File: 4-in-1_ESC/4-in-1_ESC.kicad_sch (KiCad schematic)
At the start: 12 parts, among them J5 BLDC Solder Pads

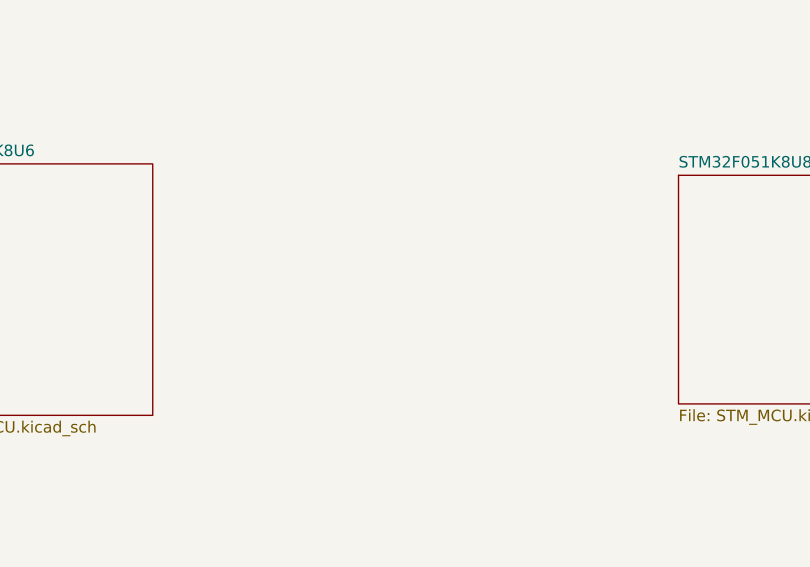
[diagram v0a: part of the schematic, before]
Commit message: Schematic Updates
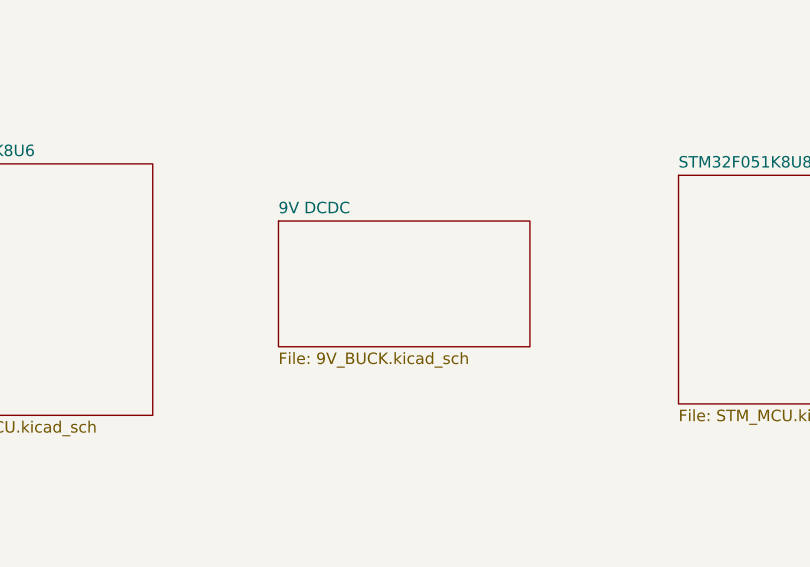
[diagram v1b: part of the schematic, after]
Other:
- added sheet 9V DCDC (9V_BUCK.kicad_sch)
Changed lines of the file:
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@@
+		)
+	)
+	(sheet
+		(at 132.08 78.74)
+		(size 27.94 13.97)
+		(exclude_from_sim no)
+		(in_bom yes)
+		(on_board yes)
+		(dnp no)
+		(fields_autoplaced yes)
+		(stroke
+			(width 0.1524)
+			(type solid)
+		)
+		(fill
+			(color 0 0 0 0)
+		)
+		(property "Sheetname" "9V DCDC"
+			(at 132.08 78.0284 0)
+			(show_name no)
+			(do_not_autoplace no)
+			(effects
+				(font
+					(size 1.27 1.27)
+				)
+				(justify left bottom)
+			)
+		)
+		(property "Sheetfile" "9V_BUCK.kicad_sch"
+			(at 132.08 93.2946 0)
+			(show_name no)
+			(do_not_autoplace no)
+			(effects
+				(font
+					(size 1.27 1.27)
+				)
+				(justify left top)
+			)
+		)
+		(instances
+			(project "4-in-1_ESC"
+				(path "/885456b2-b92d-459f-a061-5f970a420f96"
+					(page "11")
+				)
+			)
 		)
 	)

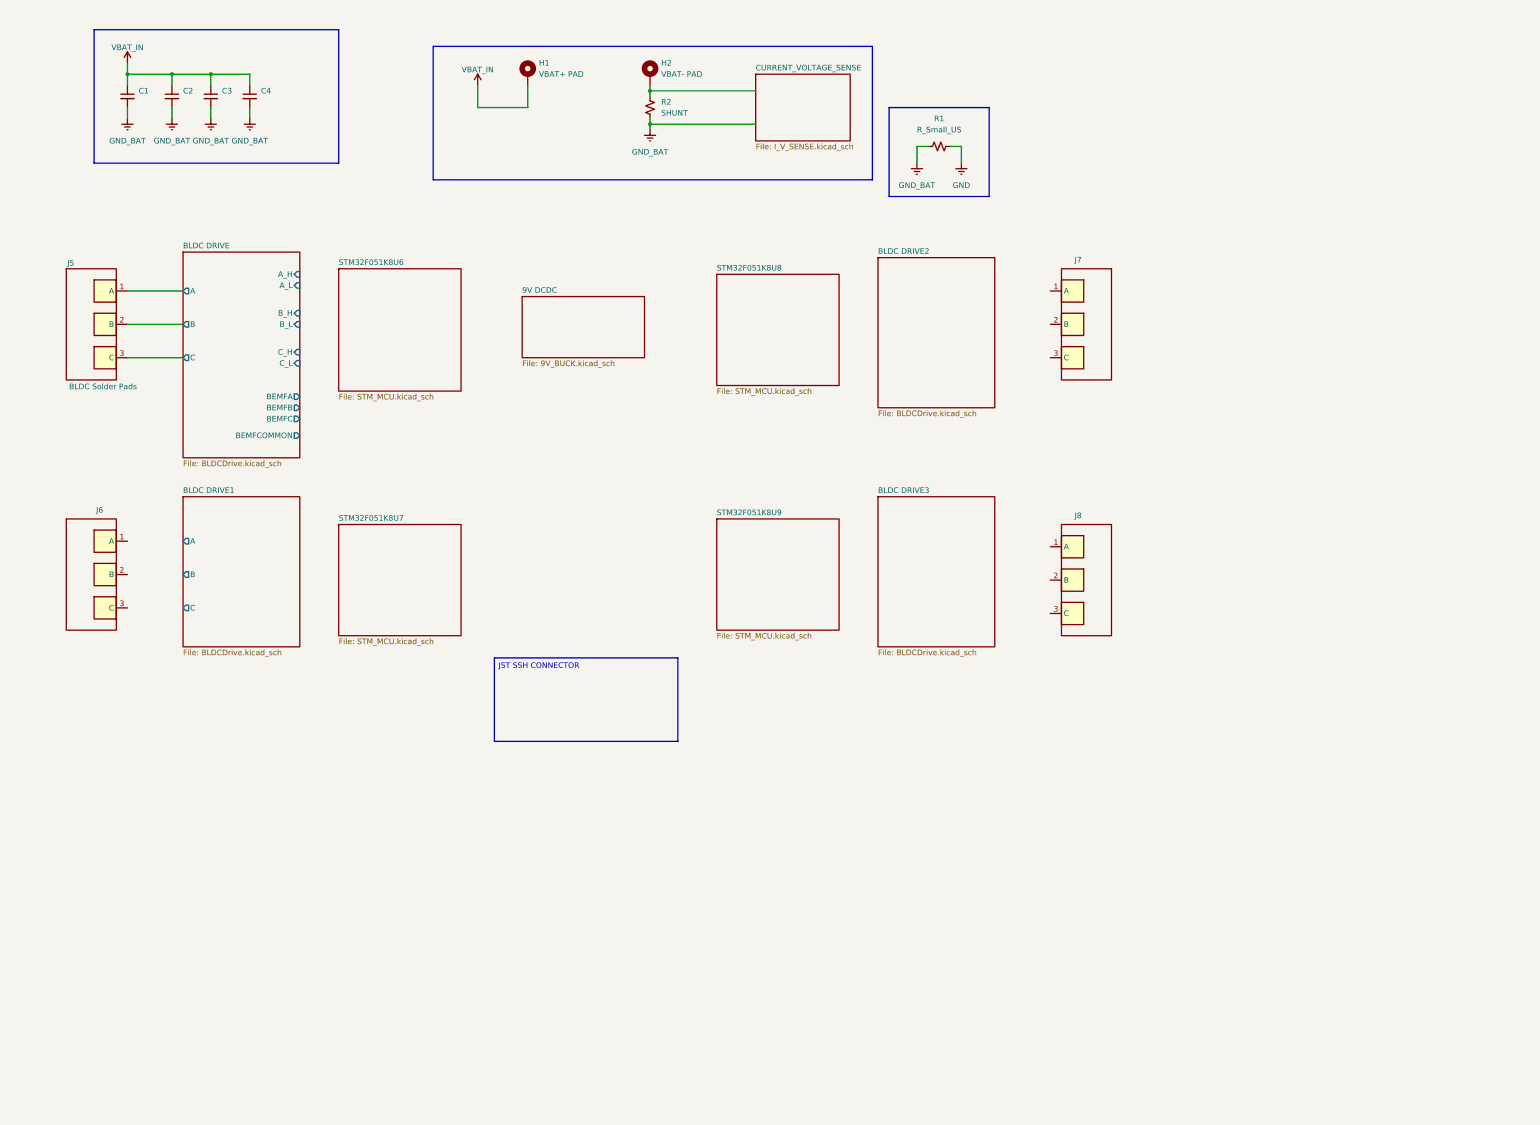
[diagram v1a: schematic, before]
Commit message: Schematic Updates
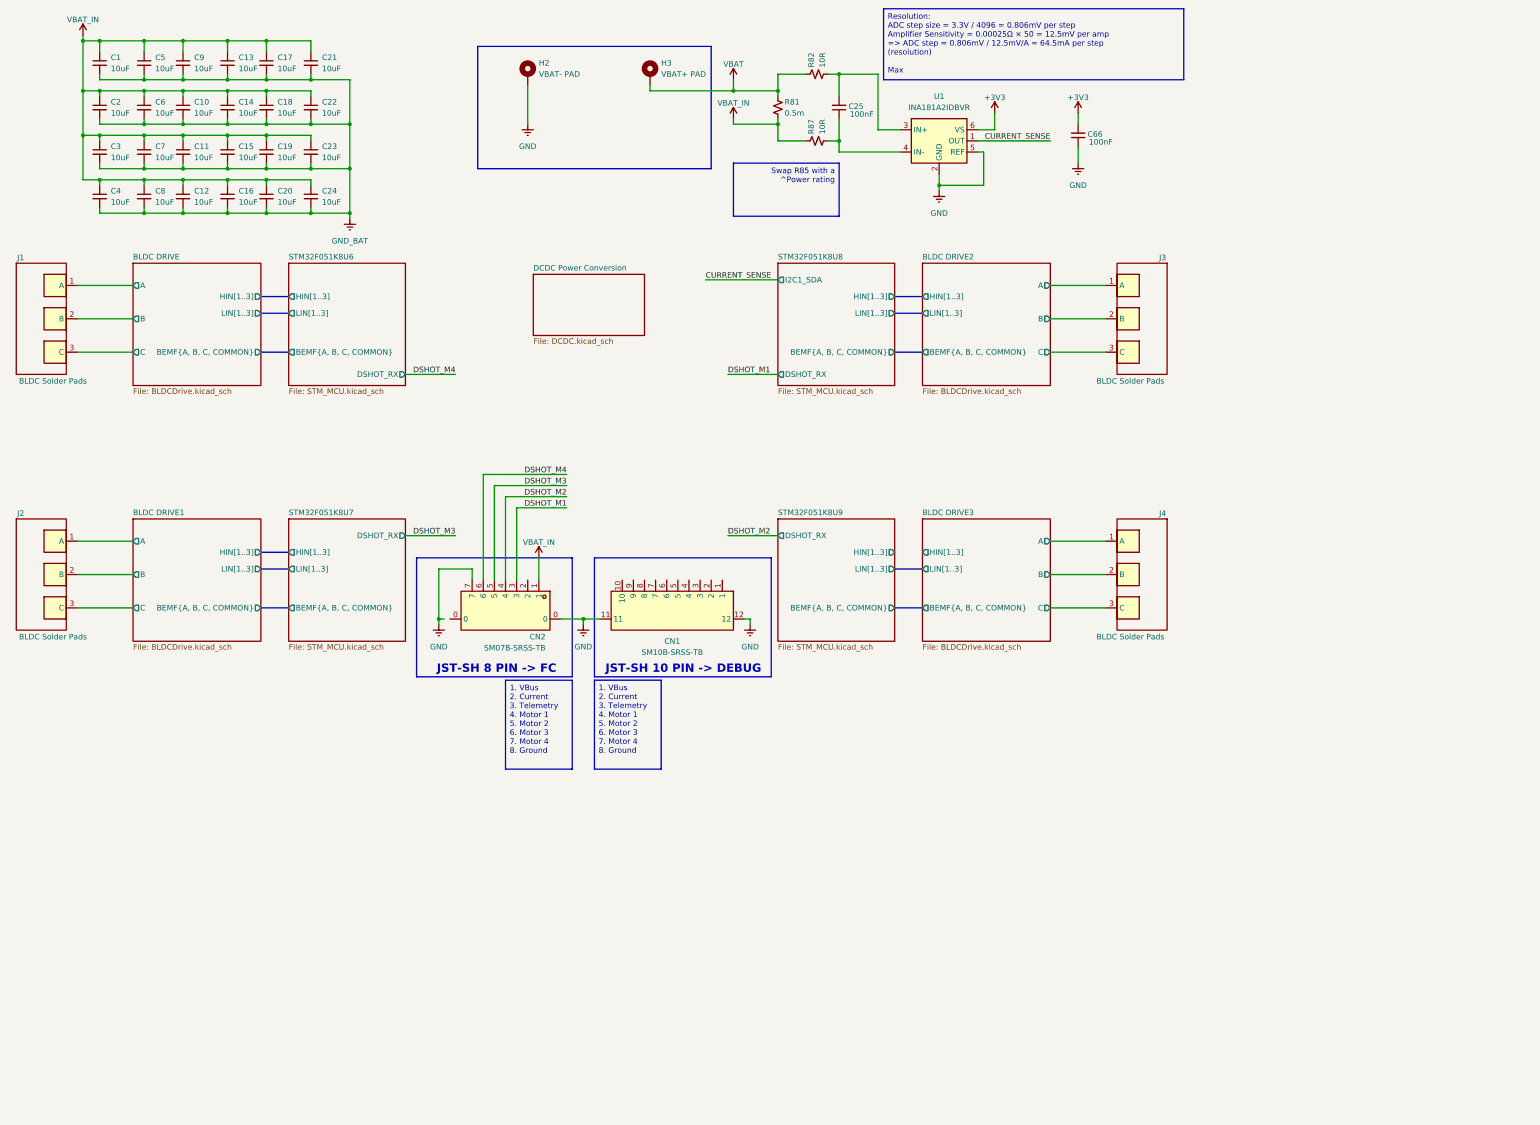
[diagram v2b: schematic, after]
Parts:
- removed H1: VBAT+ PAD, symbol Mechanical:MountingHole_Pad
- removed J6, J7, J8: (no value), symbol custom_symbols:BLDC_Solder_Pads
- removed R1: R_Small_US, symbol Device:R_Small_US
- removed R2: SHUNT, symbol Device:R_Small_US
- added C10, C11, C12, C13, C14, C15, C16, C17, C18, C19, C20, C21, C22, C23, C24, C5, C6, C7, C8, C9: 10uF, Capacitor_SMD:C_0805_2012Metric, symbol Device:C_Small
- added C25, C66: 100nF, Capacitor_SMD:C_0402_1005Metric, symbol Device:C_Small
- added CN1: SM10B-SRSS-TB, easyeda_import:CONN-SMD_10P-P1.00_SM10B-SRSS-TB-LF-SN, symbol easyeda_import:SM10B-SRSS-TB
- added CN2: SM07B-SRSS-TB, easyeda_import:CONN-SMD_SM07B-SRSS-TB, symbol easyeda_import:SM07B-SRSS-TB
- added H3: VBAT+ PAD, symbol Mechanical:MountingHole_Pad
- added J2, J3, J4: BLDC Solder Pads, symbol custom_symbols:BLDC_Solder_Pads
- added R81: 0.5m, symbol Device:R_Small_US
- added R82, R87: 10R, Resistor_SMD:R_0402_1005Metric, symbol Device:R_Small_US
- added U1: INA181A2IDBVR, easyeda_import:SOT-23-6_L2.9-W1.6-P0.95-LS2.8-BL, symbol easyeda_import:INA181A2IDBVR
- C1, C2, C3, C4: value (none) -> 10uF; footprint (none) -> Capacitor_SMD:C_0805_2012Metric
- renumbered J5 to J1
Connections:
- net BLDC DRIVE1/A: now also J2.1 (A)
- net BLDC DRIVE1/B: now also J2.2 (B)
- net BLDC DRIVE1/C: now also J2.3 (C)
- net GND: now also H2.1, C66.1, CN1.11, CN1.12, CN2.0, CN2.7, U1.2 (GND), U1.5 (REF)
- net GND_BAT: now also C10.2, C11.2, C12.2, C13.2, C14.2, C15.2, C16.2, C17.2, C18.2, C19.2, C20.2, C21.2, C22.2, C23.2, C24.2, C5.2, C6.2, C7.2, C8.2, C9.2
- net VBAT_IN: now also C10.1, C11.1, C12.1, C13.1, C14.1, C15.1, C16.1, C17.1, C18.1, C19.1, C20.1, C21.1, C22.1, C23.1, C24.1, C5.1, C6.1, C7.1, C8.1, C9.1, CN2.1, R81.2, R87.1
- new net: C25.1, R87.2, U1.4 (IN-)
- new net: C25.2, R82.2, U1.3 (IN+)
- new net +3V3: C66.2, U1.6 (VS)
- new net BLDC DRIVE2/A: J3.1 (A)
- new net BLDC DRIVE2/B: J3.2 (B)
- new net BLDC DRIVE2/C: J3.3 (C)
- new net BLDC DRIVE3/A: J4.1 (A)
- new net BLDC DRIVE3/B: J4.2 (B)
- new net BLDC DRIVE3/C: J4.3 (C)
- new net CURRENT_SENSE: U1.1 (OUT)
- new net DSHOT_M1: CN2.3
- new net DSHOT_M2: CN2.4
- new net DSHOT_M3: CN2.5
- new net DSHOT_M4: CN2.6
- new net VBAT: H3.1, R81.1, R82.1
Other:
- sheet 9V DCDC renamed DCDC Power Conversion
- removed sheet CURRENT_VOLTAGE_SENSE
- sheet BLDC DRIVE ports: added BEMF{A, B, C, COMMON}, HIN[1..3], LIN[1..3]; removed A_H, A_L, BEMFA, BEMFB, BEMFC, BEMFCOMMON, B_H, B_L, C_H, C_L
- sheet BLDC DRIVE1 ports: added BEMF{A, B, C, COMMON}, HIN[1..3], LIN[1..3]; removed none
- sheet BLDC DRIVE2 ports: added A, B, BEMF{A, B, C, COMMON}, C, HIN[1..3], LIN[1..3]; removed none
- sheet BLDC DRIVE3 ports: added A, B, BEMF{A, B, C, COMMON}, C, HIN[1..3], LIN[1..3]; removed none
- sheet DCDC Power Conversion: file 9V_BUCK.kicad_sch -> DCDC.kicad_sch
- sheet STM32F051K8U6 ports: added BEMF{A, B, C, COMMON}, DSHOT_RX, HIN[1..3], LIN[1..3]; removed none
- sheet STM32F051K8U7 ports: added BEMF{A, B, C, COMMON}, DSHOT_RX, HIN[1..3], LIN[1..3]; removed none
- sheet STM32F051K8U8 ports: added BEMF{A, B, C, COMMON}, DSHOT_RX, HIN[1..3], I2C1_SDA, LIN[1..3]; removed none
- sheet STM32F051K8U9 ports: added BEMF{A, B, C, COMMON}, DSHOT_RX, HIN[1..3], LIN[1..3]; removed none
- note added: "JST-SH 10 PIN -> DEBUG"
- note added: "JST-SH 8 PIN -> FC"
- title: (none) -> 4-in-1 ESC
- moved on the sheet: C1, J1

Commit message: Schematic First Pass
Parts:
- removed C25: 100nF, Capacitor_SMD:C_0402_1005Metric, symbol Device:C_Small
- removed R82, R87: 10R, Resistor_SMD:R_0402_1005Metric, symbol Device:R_Small_US
- added C82, C86: 10nF, Capacitor_SMD:C_0402_1005Metric, symbol Device:C_Small
- R81: value 0.5m -> 0.5m 2W
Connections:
- net +3V3: now also CN1.1
- net GND: now also CN1.10, C82.1, C86.1
- net VBAT: now also U1.3 (IN+), C86.2
- net VBAT_IN: now also U1.4 (IN-), C82.2
- net KISS_TELEM: now reaches CN2.2
- net SWDIO_M1: now reaches CN1.2
- net SWCLK_M1: now reaches CN1.3
- net SWDIO_M2: now reaches CN1.4
- net SWCLK_M2: now reaches CN1.5
- net SWDIO_M3: now reaches CN1.6
- net SWCLK_M3: now reaches CN1.7
- net SWDIO_M4: now reaches CN1.8
- net SWCLK_M4: now reaches CN1.9
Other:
- sheet DCDC Power Conversion renamed 10V BUCK & 3V3 LDO
- sheet STM32F051K8U6 ports: added SWCLK, SWDIO; removed none
- sheet STM32F051K8U7 ports: added SWCLK, SWDIO; removed none
- sheet STM32F051K8U8 ports: added CURRENT_SENSE, KISS_TELEM, SWCLK, SWDIO; removed I2C1_SDA
- sheet STM32F051K8U9 ports: added SWCLK, SWDIO; removed none
- note added: "3S-8S"
- note added: "3S-8S BATTERY"
- note added: "BLDC_MOTOR_1"
- note added: "BLDC_MOTOR_2"
- note added: "BLDC_MOTOR_3"
- note added: "BLDC_MOTOR_4"
- note added: "FATALAS 4-IN-1 ESC"
- moved on the sheet: C1, C10, C11, C12, C13, C14, C15, C16, C17, C18, C19, C2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
